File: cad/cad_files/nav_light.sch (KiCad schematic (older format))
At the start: 1 part

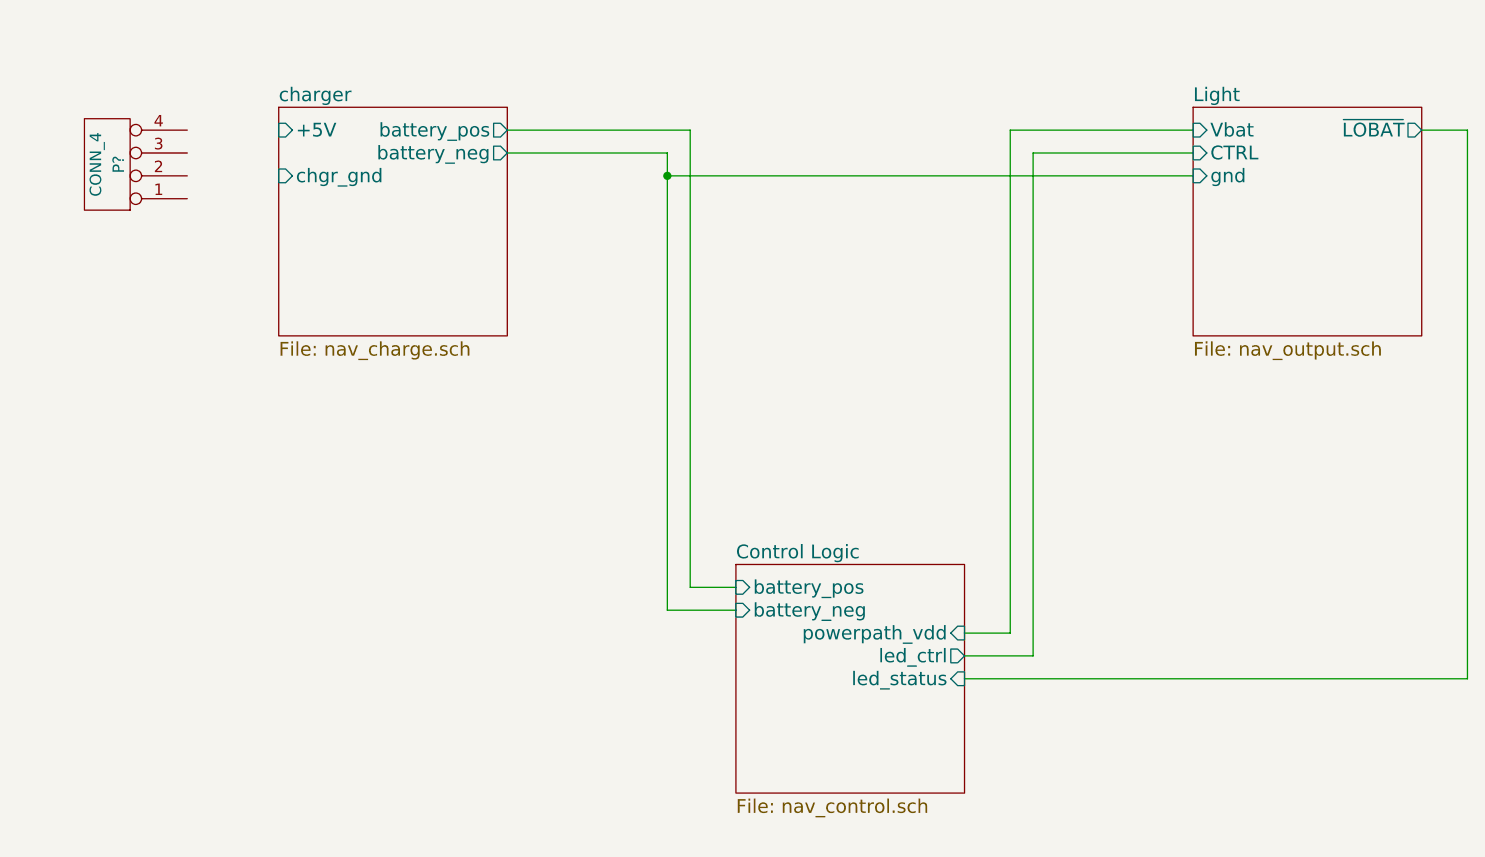
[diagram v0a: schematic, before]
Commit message: Bring charge status signal to control logic
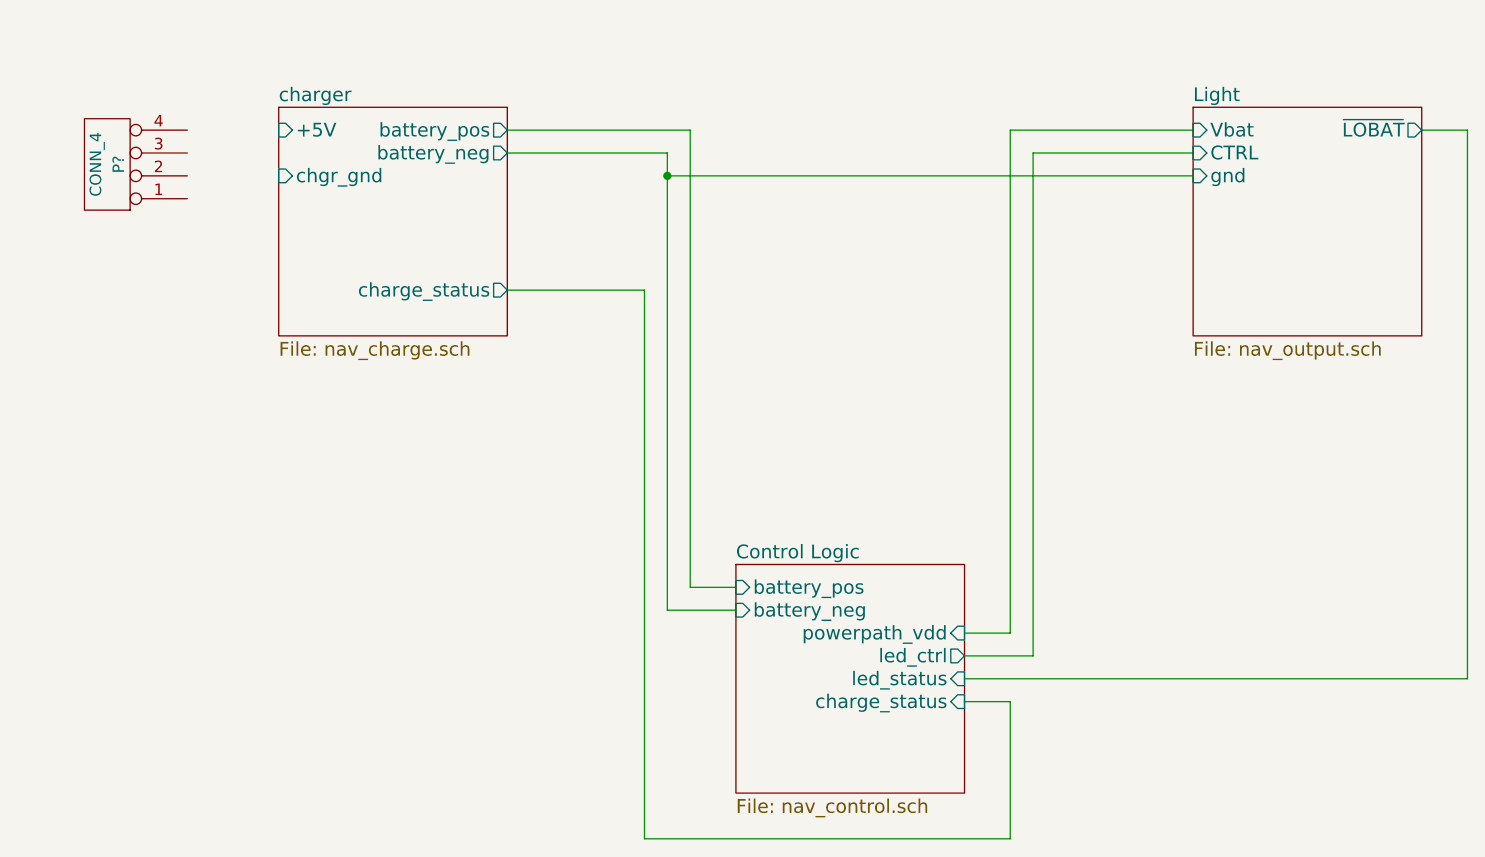
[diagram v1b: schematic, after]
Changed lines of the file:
@@
-EESchema Schematic File Version 2  date Tue 02 Dec 2014 10:18:06 PM HST
+EESchema Schematic File Version 2  date Tue 02 Dec 2014 11:37:56 PM HST
 LIBS:local_parts
 LIBS:power
@@
 Comment4 ""
 $EndDescr
-Connection ~ 4200 2800
+Wire Wire Line
+	5500 5100 5700 5100
+Wire Wire Line
+	5700 5100 5700 5700
+Wire Wire Line
+	5700 5700 4100 5700
+Wire Wire Line
+	4100 5700 4100 3300
+Wire Wire Line
+	4100 3300 3500 3300
+Wire Wire Line
+	7500 2600 7700 2600
+Wire Wire Line
+	7700 2600 7700 5000
+Wire Wire Line
+	7700 5000 5500 5000
+Wire Wire Line
+	6500 2600 5700 2600
+Wire Wire Line
+	5700 2600 5700 4800
+Wire Wire Line
+	5700 4800 5500 4800
+Wire Wire Line
+	4500 4600 4300 4600
+Wire Wire Line
+	4300 4600 4300 2600
+Wire Wire Line
+	4300 2600 3500 2600
+Wire Wire Line
+	3500 2700 4200 2700
+Wire Wire Line
+	4200 2700 4200 4700
+Wire Wire Line
+	4200 4700 4500 4700
+Wire Wire Line
+	5500 4900 5800 4900
+Wire Wire Line
+	5800 4900 5800 2700
+Wire Wire Line
+	5800 2700 6500 2700
 Wire Wire Line
 	4200 2800 6500 2800
-Wire Wire Line
-	6500 2700 5800 2700
-Wire Wire Line
-	5800 2700 5800 4900
-Wire Wire Line
-	5800 4900 5500 4900
-Wire Wire Line
-	4500 4700 4200 4700
-Wire Wire Line
-	4200 4700 4200 2700
-Wire Wire Line
-	4200 2700 3500 2700
-Wire Wire Line
-	3500 2600 4300 2600
-Wire Wire Line
-	4300 2600 4300 4600
-Wire Wire Line
-	4300 4600 4500 4600
-Wire Wire Line
-	5500 4800 5700 4800
-Wire Wire Line
-	5700 4800 5700 2600
-Wire Wire Line
-	5700 2600 6500 2600
-Wire Wire Line
-	5500 5000 7700 5000
-Wire Wire Line
-	7700 5000 7700 2600
-Wire Wire Line
-	7700 2600 7500 2600
+Connection ~ 4200 2800
 $Sheet
 S 4500 4500 1000 1000
@@
 F5 "battery_pos" I L 4500 4600 60
 F6 "powerpath_vdd" I R 5500 4800 60
+F7 "charge_status" I R 5500 5100 60
 $EndSheet
 $Sheet
@@
 F4 "chgr_gnd" I L 2500 2800 60
 F5 "+5V" I L 2500 2600 60
+F6 "charge_status" O R 3500 3300 60
 $EndSheet
 $Sheet

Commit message: Change power input to 2-pin part
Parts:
- removed P?: CONN_4, symbol CONN_4
- added Pp101: CONN_2, symbol CONN_2
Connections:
- wire segments 21 -> 23
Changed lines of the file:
@@
-EESchema Schematic File Version 2  date Wed 03 Dec 2014 05:34:03 PM HST
+EESchema Schematic File Version 2  date Wed 03 Dec 2014 05:36:01 PM HST
 LIBS:local_parts
 LIBS:power
@@
 $EndDescr
 Wire Wire Line
+	2300 2800 2500 2800
+Wire Wire Line
 	5500 5100 5700 5100
 Wire Wire Line
@@
 	4200 2800 6500 2800
 Connection ~ 4200 2800
+Wire Wire Line
+	2300 2600 2500 2600
+$Comp
+L CONN_2 Pp101
+U 1 1 547FD67C
+P 1950 2700
+F 0 "Pp101" V 1900 2700 40  0000 C CNN
+F 1 "CONN_2" V 2000 2700 40  0000 C CNN
+	1    1950 2700
+	-1   0    0    1
+$EndComp
 $Sheet
 S 4500 4500 1000 1000
@@
 F5 "Vbat" I L 6500 2600 60
 $EndSheet
-$Comp
-L CONN_4 P?
-U 1 1 53D0DAAF
-P 1750 2750
-F 0 "P?" V 1700 2750 50  0000 C CNN
-F 1 "CONN_4" V 1800 2750 50  0000 C CNN
-	1    1750 2750
-	-1   0    0    1
-$EndComp
 $EndSCHEMATC
